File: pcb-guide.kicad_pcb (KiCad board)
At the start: 2 copper layers, 20 parts, among them SW1 SW_Push, U1 ATmega32U4-AU, Y1 16Mhz

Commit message: part 5 almost finished
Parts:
- added MX1: MX-NoLED, MX_Alps_Hybrid:MX-1U, F.Cu at (214.3, 39.7)
- added MX2: MX-NoLED, MX_Alps_Hybrid:MX-1U, F.Cu at (233.4, 39.7)
- added MX3: MX-NoLED, MX_Alps_Hybrid:MX-1U, F.Cu at (214.3, 58.7)
- added MX4: MX-NoLED, MX_Alps_Hybrid:MX-1U, F.Cu at (233.4, 58.7)
- C1, C2, C3, C4, C5, C6, C7, D1, D2, D3, D4, R1, U1, Y1: moved to B.Cu
- moved D4 113.4 mm to (241.3, 58.7), turned to 90 degrees
- moved D2 99.7 mm to (241.3, 39.7), turned to 90 degrees
- moved D3 99.2 mm to (222.2, 58.7), turned to 90 degrees
- moved D1 82.3 mm to (222.2, 39.7), turned to 90 degrees
- moved C2 79.7 mm to (194.5, 64.2), turned to 90 degrees
- moved U1 79.2 mm to (190.5, 50.8), turned to 180 degrees
- moved C4 77.4 mm to (198.4, 59.4), turned to 270 degrees
- moved Y1 75.5 mm to (190.0, 64.3)
- moved R1 74.5 mm to (201.6, 59.4), turned to 270 degrees
- moved C3 74.4 mm to (200.7, 51.6)
- moved C1 71.2 mm to (185.7, 64.3), turned to 270 degrees
- moved R3 68.6 mm to (228.5, -1.59)
- moved R4 66.9 mm to (221.3, 3.17)
- moved C5 65.3 mm to (181.0, 55.4), turned to 270 degrees
- moved F1 65.2 mm to (220.1, -14.3)
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
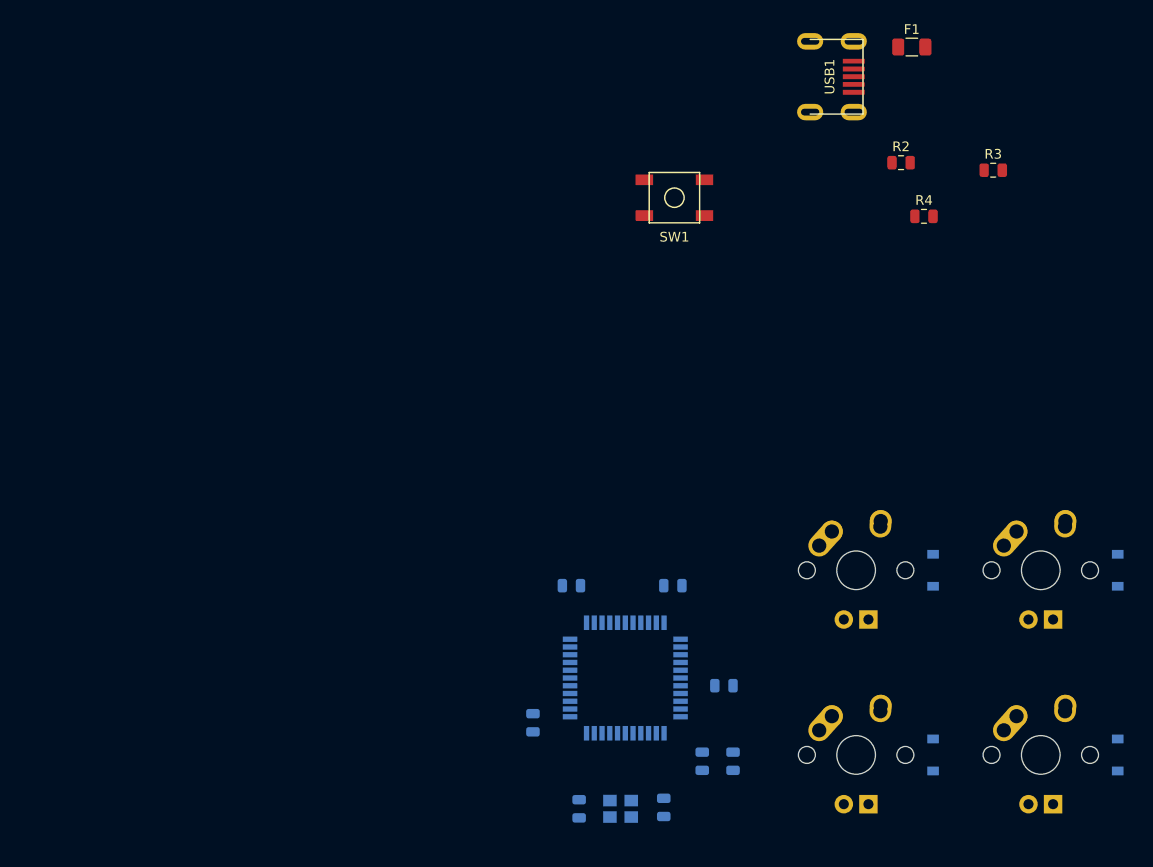
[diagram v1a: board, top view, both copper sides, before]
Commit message: Board setup added and R joints finished
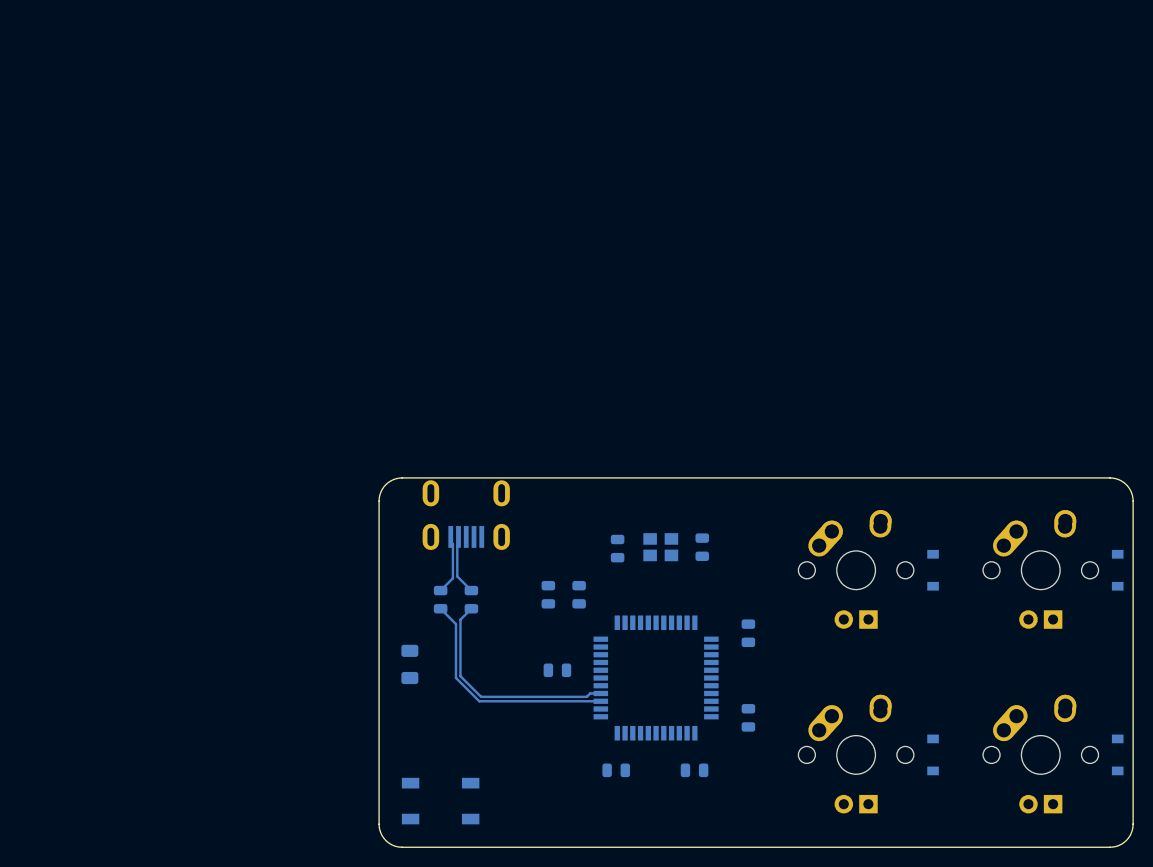
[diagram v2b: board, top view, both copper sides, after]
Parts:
- F1, R2, R3, R4, SW1, USB1: moved to B.Cu
- moved F1 82.1 mm to (168.3, 49.4), turned to 270 degrees
- moved R3 72.2 mm to (171.4, 42.7), turned to 90 degrees
- moved SW1 66.8 mm to (171.4, 63.5), turned to 180 degrees
- moved R2 63.2 mm to (174.6, 42.7), turned to 90 degrees
- moved USB1 55.7 mm to (174.1, 31.8), turned to 270 degrees
- moved R4 54.8 mm to (203.2, 54.9), turned to 90 degrees
- moved C1 29.8 mm to (198.4, 37.3), turned to 90 degrees
- moved Y1 27.3 mm to (194.2, 37.3), turned to 180 degrees
- moved C2 27.1 mm to (189.7, 37.5), turned to 270 degrees
- moved R1 25.6 mm to (182.6, 42.2), turned to 90 degrees
- moved C5 24.1 mm to (203.2, 46.2), turned to 90 degrees
- moved C6 22.9 mm to (197.6, 60.3), turned to 180 degrees
- moved C4 21.4 mm to (185.7, 42.2), turned to 90 degrees
- moved C7 19.9 mm to (189.6, 60.3), turned to 0 degrees
- moved C3 17.2 mm to (183.5, 50.0), turned to 180 degrees
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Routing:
- net Net-(R3-Pad1): track 0.00 -> 23.7 mm
- net Net-(R2-Pad1): track 0.00 -> 22.9 mm
- net D+: track 0.00 -> 6.18 mm
- net D-: track 0.00 -> 6.15 mm
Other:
- net class Default: trace_width 0.25 -> 0.254
- net class Power added: clearance 0.2, trace_width 0.381, via_dia 0.8, via_drill 0.4

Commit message: Se termina el enrutamiento de los componentes
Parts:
- moved C7 7.45 mm to (183.4, 56.2), turned to 270 degrees
- turned F1 to 90 degrees
- turned R1 to 270 degrees
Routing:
- net GND: track 0.00 -> 150.1 mm
- net +5V: track 0.00 -> 102.6 mm, vias 0 -> 5
- net Net-(R1-Pad2): track 0.00 -> 35.4 mm, vias 0 -> 2
- net ROW1: track 0.00 -> 20.3 mm
- net ROW0: track 0.00 -> 20.3 mm
- net COL1: track 0.00 -> 19.0 mm, vias 0 -> 1
- net COL0: track 0.00 -> 19.0 mm, vias 0 -> 3
- net Net-(C2-Pad1): track 0.00 -> 12.9 mm
- net VCC: track 0.00 -> 12.6 mm
- net Net-(C1-Pad1): track 0.00 -> 10.9 mm
- net Net-(D3-Pad2): track 0.00 -> 7.86 mm
- net Net-(D4-Pad2): track 0.00 -> 7.71 mm
- net Net-(D1-Pad2): track 0.00 -> 7.51 mm
- net Net-(D2-Pad2): track 0.00 -> 7.51 mm
- net Net-(R4-Pad2): track 0.00 -> 4.17 mm
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
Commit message: Finish
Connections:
- U1 pad 27: Net-(U1-Pad27) -> ROW0
- U1 pad 28: Net-(U1-Pad28) -> COL1
- U1 pad 29: Net-(U1-Pad29) -> COL0
- U1 pad 30: Net-(U1-Pad30) -> ROW1
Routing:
- net COL1: track 19.0 -> 51.5 mm
- net ROW1: track 20.3 -> 51.3 mm
- net ROW0: track 20.3 -> 47.2 mm
- net COL0: track 19.0 -> 32.1 mm

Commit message: Agregamos la placa de GND a las partes delicadas
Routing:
- added copper zone on B.Cu, net GND
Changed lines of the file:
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@@
   (segment (start 224.155 50.8) (end 229.5525 56.1975) (width 0.254) (layer B.Cu) (net 44))
   (segment (start 199.375 50.8) (end 224.155 50.8) (width 0.254) (layer B.Cu) (net 44))
+  (zone (net 1) (net_name GND) (layer B.Cu) (hatch edge 0.508)
+    (connect_pads (clearance 0.508))
+    (min_thickness 0.254)
+    (fill yes (arc_segments 32) (thermal_gap 0.508) (thermal_bridge_width 0.508))
+    (polygon
+      (pts
+        (xy 202.40625 33.3375) (xy 186.53125 33.3375) (xy 186.53125 41.275) (xy 202.40625 41.275)
+      )
+    )
+  )
+  (zone (net 1) (net_name GND) (layer B.Cu) (hatch edge 0.508)
+    (connect_pads (clearance 0.508))
+    (min_thickness 0.254)
+    (fill yes (arc_segments 32) (thermal_gap 0.508) (thermal_bridge_width 0.508))
+    (polygon
+      (pts
+        (xy 188.9125 46.0375) (xy 198.4375 46.0375) (xy 198.4375 55.5625) (xy 188.9125 55.5625)
+      )
+    )
+  )
+  (zone (net 1) (net_name GND) (layer B.Cu) (hatch edge 0.508)
+    (connect_pads (clearance 0.508))
+    (min_thickness 0.254)
+    (fill yes (arc_segments 32) (thermal_gap 0.508) (thermal_bridge_width 0.508))
+    (polygon
+      (pts
+        (xy 177.8 30.1625) (xy 170.65625 30.1625) (xy 170.65625 37.30625) (xy 177.8 37.30625)
+      )
+    )
+  )
 )

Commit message: PCB finished
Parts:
- MX1, MX2, MX3, MX4: footprint MX_Alps_Hybrid:MX-1U -> MX_Only:MXOnly-1U
- moved C2 4.70 mm to (189.7, 32.8)
- moved C6 4.70 mm to (197.6, 55.6)
- moved C1 4.70 mm to (198.4, 32.6)
- moved C3 4.70 mm to (183.5, 45.3)
- moved C4 4.70 mm to (185.7, 37.5)
- moved C5 4.70 mm to (203.2, 41.5)
- moved C7 4.70 mm to (183.4, 51.5)
- moved D1 4.70 mm to (222.2, 35.0)
- moved D2 4.70 mm to (241.3, 35.0)
- moved D3 4.70 mm to (222.2, 54.0)
- moved D4 4.70 mm to (241.3, 54.0)
- moved F1 4.70 mm to (168.3, 44.7)
- moved MX1 4.70 mm to (214.3, 35.0)
- moved MX2 4.70 mm to (233.4, 35.0)
- moved MX3 4.70 mm to (214.3, 54.0)
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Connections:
- USB1 pad 3: Net-(USB1-Pad3) -> D+
- USB1 pad 4: D+ -> D-
- USB1 pad 5: D- -> VCC
- USB1 pad 6: VCC -> Net-(USB1-Pad6)
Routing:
- net VCC: track 12.6 -> 14.1 mm
- net D-: track 6.15 -> 7.25 mm
- net D+: track 6.18 -> 5.64 mm
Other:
- board outline added: 77.8 x 38.1 mm
- rule trace_min: 0.2 -> 0
